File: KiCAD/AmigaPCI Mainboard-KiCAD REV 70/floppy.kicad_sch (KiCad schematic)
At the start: 30 parts, among them CN203 DB25_Stack_FemaleAndMale, CN204 INTERNAL FLOPPY, J200 SHORT FOR DF1, J201 1-2 AMIGA DRIVES/2-3 PC DRIVES, J202 1-2 AMIGA DRIVES/2-3 PC DRIVES, J207 TICK, J208 TBASE, U204 8520, U209 74HCT08, U212 74HCT74, U213 74HCT00, U215 74HC03, U305 74HCT08

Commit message: Add JLCPCB part numbers and fix 74LVC244 footprints.
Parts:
- C241, C243, C252, C256: LCSC (none) -> C14663
- CN203: LCSC (none) -> C17554757
- CN204: LCSC (none) -> C2685134
- D206, D207, D208, D209, D210, D212: LCSC (none) -> C37574382
- D301: LCSC (none) -> C460736
- FB202: LCSC (none) -> C2762183
- J200: LCSC (none) -> C124375
- J201, J202, J207, J208: LCSC (none) -> C49257
- R225: LCSC (none) -> C21190
- R237: LCSC (none) -> C23182
- R310: LCSC (none) -> C560533
- RN211: LCSC (none) -> C309679
- RN305: LCSC (none) -> C1731268
- U204: LCSC (none) -> C2332
- U209, U305: LCSC (none) -> C131488
- U212: LCSC (none) -> C141335
- U213: LCSC (none) -> C8206
- U215: LCSC (none) -> C546492

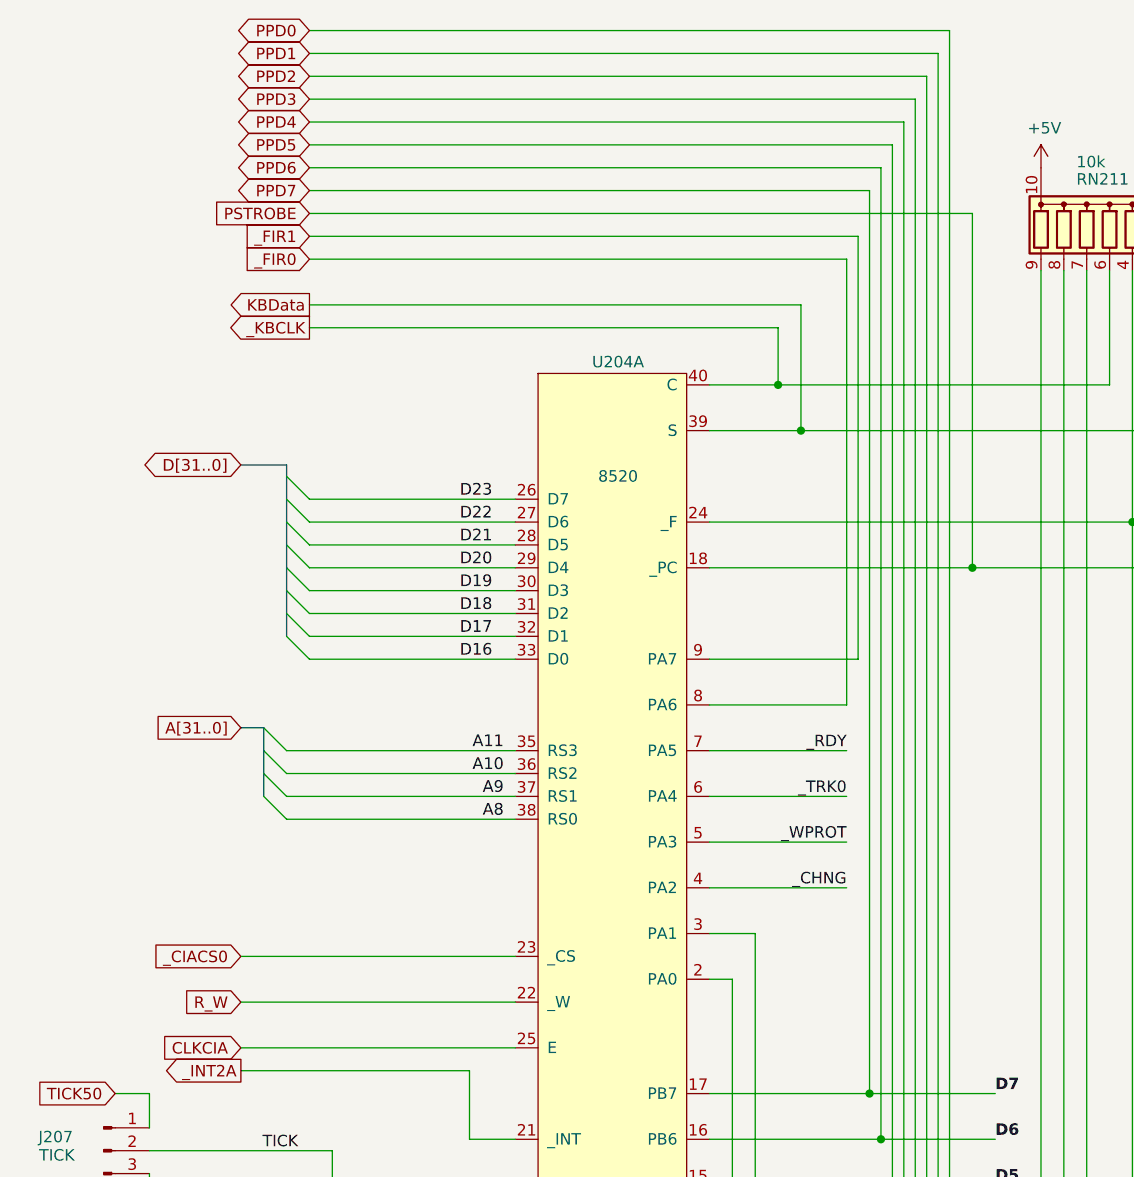
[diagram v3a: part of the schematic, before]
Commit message: Updates to revision 7 board.
Change U810 to 74LVC245 buffers
Add CDAC to U712
Add address latch to CIAs
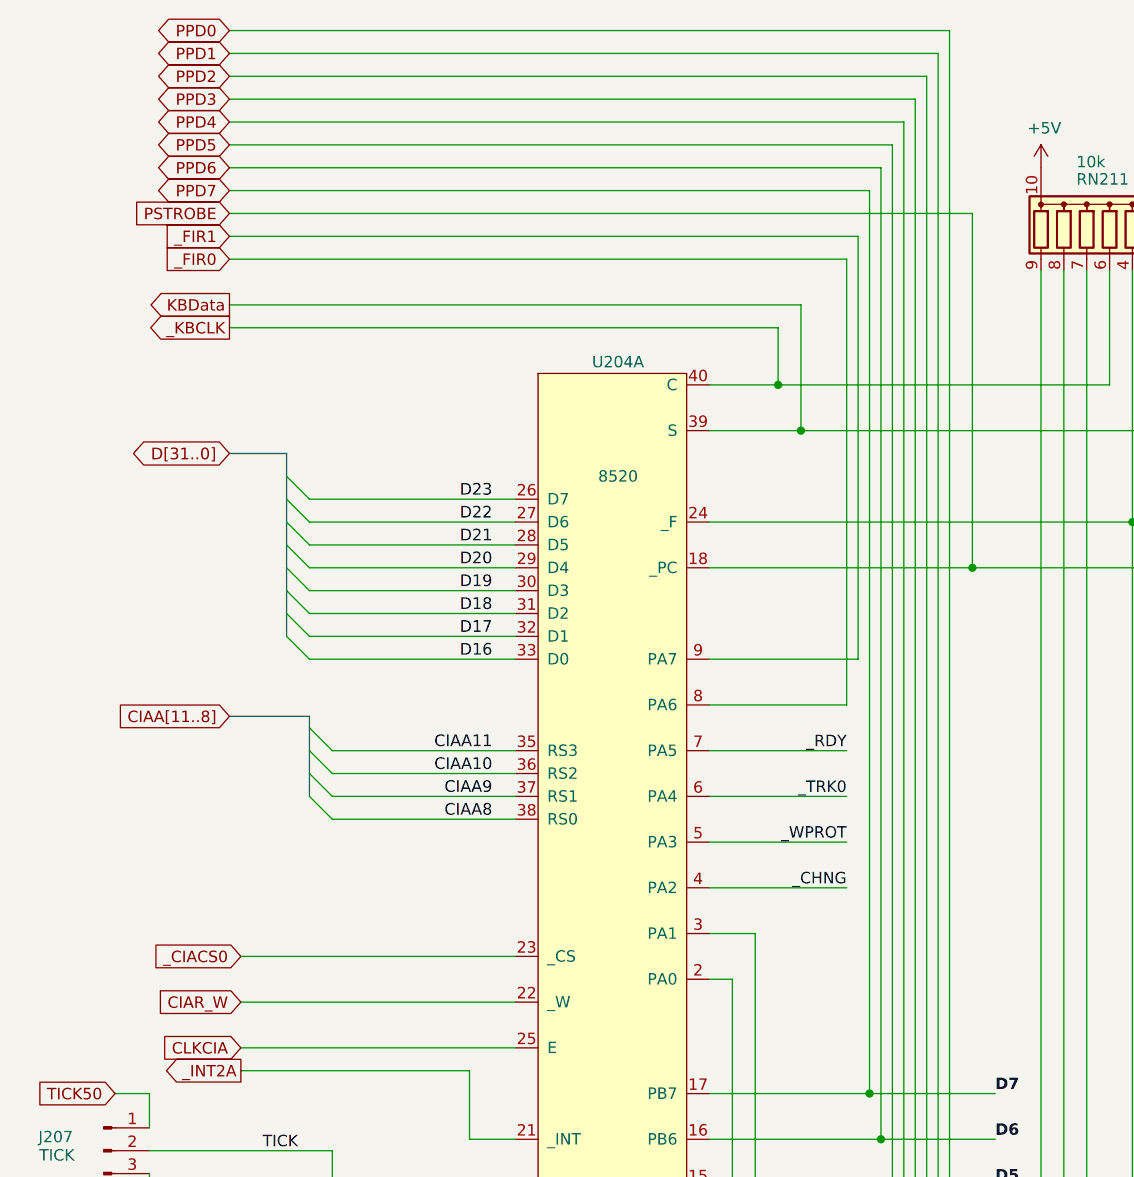
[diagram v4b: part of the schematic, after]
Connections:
- net A10 renamed CIAA10
- net A11 renamed CIAA11
- net A8 renamed CIAA8
- net A9 renamed CIAA9
- net R_W renamed CIAR_W

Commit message: New hardware rev files.
Gerber
BOM w/JLCPCB part numbers
Pick-n-Place File
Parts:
- U215: LCSC C546492 -> C2869660
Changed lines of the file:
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@@
 			)
 		)
-		(property "LCSC" "C546492"
+		(property "LCSC" "C2869660"
 			(at 304.8 39.37 0)
 			(effects
@@
 			)
 		)
-		(property "LCSC" "C546492"
+		(property "LCSC" "C2869660"
 			(at 303.53 54.61 0)
 			(effects
@@
 			)
 		)
-		(property "LCSC" "C546492"
+		(property "LCSC" "C2869660"
 			(at 166.37 238.76 0)
 			(effects
